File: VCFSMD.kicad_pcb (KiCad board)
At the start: 2 copper layers, 138.4 x 128 mm, 116 parts, among them J1 Conn_01x06_Pin, J10 AudioJack2, J11 AudioJack2, J12 AudioJack2, J13 AudioJack2, J14 Conn_01x06_Pin, J2 Conn_02x05_Odd_Even, J3 Conn_01x07_Pin, J4 Conn_01x07_Pin, J5 AudioJack2, J6 AudioJack2, J7 AudioJack2, J8 AudioJack2, J9 AudioJack2, Q1 BC857, Q2 BC857, Q3 BC847, SW1 SW_SPDT, U1 TL074, U2 L7809, U3 TL074, U4 TL074, U5 LM13700, U6 LM7909_TO220

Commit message: Add files via upload
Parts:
- removed C6, C8: 1u, Capacitor_SMD:C_1206_3216Metric
- removed J1, J14: Conn_01x06_Pin, Connector_PinHeader_2.54mm:PinHeader_1x06_P2.54mm_Vertical
- removed J3, J4: Conn_01x07_Pin, Connector_PinHeader_2.54mm:PinHeader_1x07_P2.54mm_Vertical
- removed U2: L7809, Package_TO_SOT_SMD:SOT-223
- removed U6: LM7909_TO220, Package_TO_SOT_SMD:SOT-223
- added ?: , , F.Cu at (126.6, 63.9)
- added ?: , , F.Cu at (176.2, 63.9)
- added C101: 10u, Capacitor_SMD:C_1206_3216Metric, F.Cu at (181.8, 118.8)
- added C102: 10u, Capacitor_SMD:C_1206_3216Metric, F.Cu at (207.7, 118.5)
- added C103: 10u, Capacitor_SMD:C_1206_3216Metric, F.Cu at (202.6, 118.6)
- added C104: 10u, Capacitor_SMD:C_1206_3216Metric, F.Cu at (184.3, 118.8)
- added J101: Conn_01x08_Pin, Connector_PinSocket_2.54mm:PinSocket_1x08_P2.54mm_Vertical, F.Cu at (182.7, 61.3)
- added J102: Conn_01x09_Pin, Connector_PinHeader_2.54mm:PinHeader_1x09_P2.54mm_Vertical, F.Cu at (127.0, 89.3)
- added J103: Conn_01x09_Pin, Connector_PinHeader_2.54mm:PinHeader_1x09_P2.54mm_Vertical, F.Cu at (176.3, 89.4)
- added J104: Conn_01x08_Pin, Connector_PinSocket_2.54mm:PinSocket_1x08_P2.54mm_Vertical, F.Cu at (133.1, 61.3)
- added R101: 1k, Resistor_SMD:R_1206_3216Metric, F.Cu at (200.1, 118.6)
- added R102: 6k2, Resistor_SMD:R_1206_3216Metric, F.Cu at (205.1, 118.6)
- added R103: 6k2, Resistor_SMD:R_1206_3216Metric, F.Cu at (176.9, 118.8)
- added R104: 1k, Resistor_SMD:R_1206_3216Metric, F.Cu at (179.2, 118.8)
- added U101: LM317_SOT-223, Package_TO_SOT_SMD:SOT-223-3_TabPin2, F.Cu at (204.4, 112.3)
- added U102: LM337_SOT223, Package_TO_SOT_SMD:SOT-223-3_TabPin2, F.Cu at (179.0, 112.4)
- C4, C7, D2, Q3, R12, R28, R31, R35, R4, R42, U3: moved to F.Cu
- moved R28 93.0 mm to (185.2, 48.3), turned to 0 degrees
- moved R12 84.9 mm to (185.2, 46.0), turned to 0 degrees
- moved Q3 83.2 mm to (189.9, 47.0), turned to 180 degrees
- moved C7 79.0 mm to (185.2, 55.1)
- moved R42 78.9 mm to (185.2, 57.6), turned to 180 degrees
- moved R31 78.9 mm to (185.2, 50.7), turned to 0 degrees
- moved D2 78.8 mm to (185.1, 52.9), turned to 180 degrees
- moved C4 73.9 mm to (197.1, 55.7), turned to -90 degrees
- moved R4 71.4 mm to (198.8, 65.0)
- moved R35 67.9 mm to (194.7, 47.1), turned to 0 degrees
- moved U3 57.6 mm to (191.7, 54.2)
- moved D4 5.42 mm to (185.6, 107.5), turned to 180 degrees
- moved R24 5.24 mm to (128.2, 57.7)
- moved RV1 5.11 mm to (131.0, 101.9)
- moved D1 5.11 mm to (139.4, 54.6)
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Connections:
- net Net-(SW1-B) renamed SW12
- C7 pad 1: Net-(C7-Pad1) -> Net-(D2-A)
- C7 pad 2: Net-(D2-A) -> PINGIN
- D11 pad 1: Net-(D11-K) -> GND
- D11 pad 2: Net-(D11-A) -> PINGLED
- J9 pad T: Net-(C7-Pad1) -> PINGIN
- Q3 pad 2: Net-(D11-A) -> Net-(Q3-E)
- R12 pad 1: GND -> PINGLED
- R12 pad 2: Net-(D11-K) -> Net-(Q3-E)
- R42 pad 1: Net-(C7-Pad1) -> PINGIN
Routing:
- net PINGLED: track 0.00 -> 94.2 mm, vias 0 -> 3
- net PINGIN: track 0.00 -> 81.2 mm, vias 0 -> 1
- net BP: track 170.7 -> 118.0 mm, vias 2 -> 5
- net VGNDAUD: track 48.0 -> 11.8 mm, vias 2 -> 0
- net AUDSUM: track 60.9 -> 95.7 mm, vias 0 -> 4
- net GND: track 26.8 -> 58.5 mm, vias 6 -> 8
- net OUT_BP: track 41.2 -> 71.3 mm, vias 1 -> 5
- net OUT_LP: track 34.2 -> 59.8 mm, vias 1 -> 2
- net -9V: track 131.9 -> 155.5 mm, vias 5 -> 7
- net Net-(D11-K): track 22.8 -> 0.00 mm, vias 1 -> 0
- net Net-(U101-ADJ): track 0.00 -> 21.6 mm, vias 0 -> 3
- net Net-(D11-A): track 18.1 -> 0.00 mm, vias 1 -> 0
- net +12V: track 11.5 -> 26.5 mm, vias 0 -> 2
- net AUDIN: track 58.3 -> 72.2 mm
- net +9V: track 31.1 -> 42.5 mm, vias 9 -> 13
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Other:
- board size 138.4 x 128 mm -> 141 x 128 mm

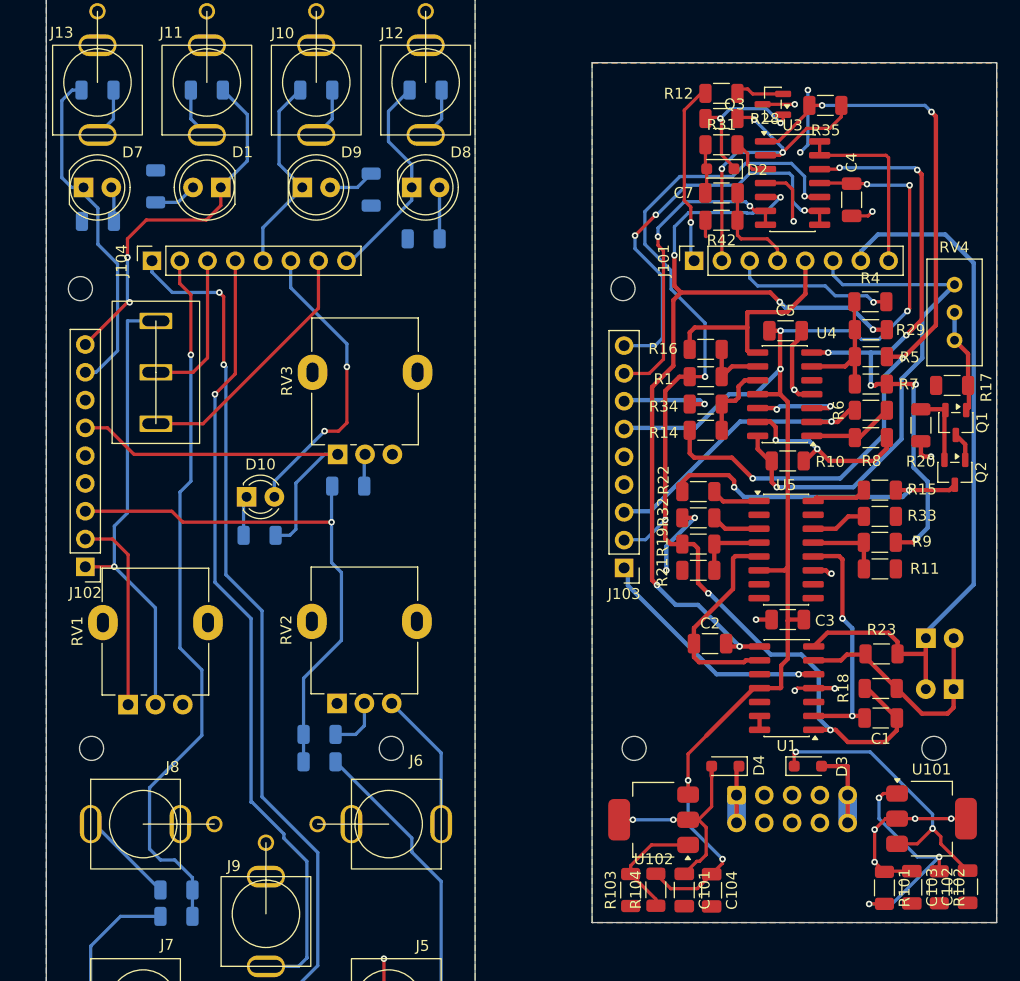
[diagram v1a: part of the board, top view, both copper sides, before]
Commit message: Changed mounting holes for spacers from M2 to M2.5
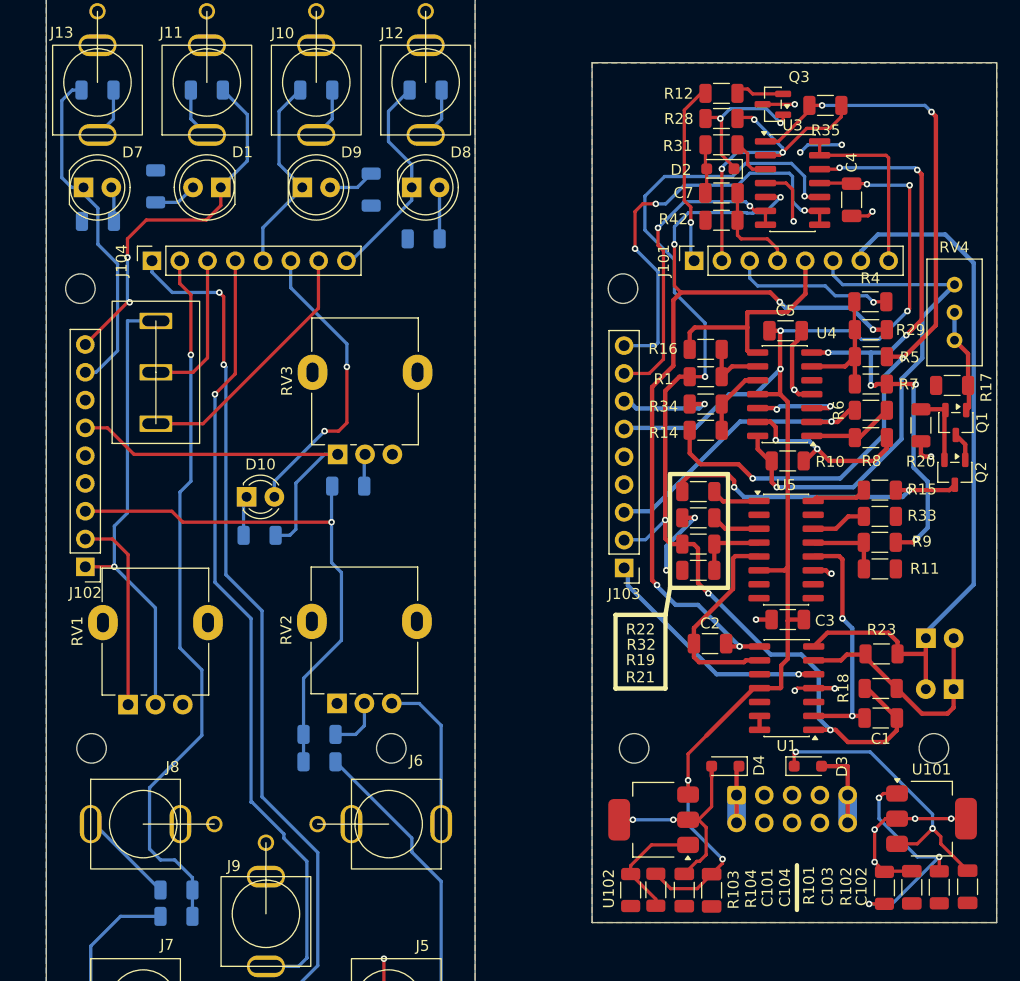
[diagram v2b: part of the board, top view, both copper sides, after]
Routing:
- net GND: track 58.5 -> 55.4 mm
- net Net-(J6-PadT): track 12.9 -> 14.4 mm
- net OUT_BP: track 71.3 -> 72.3 mm
- net BP: track 118.0 -> 118.8 mm

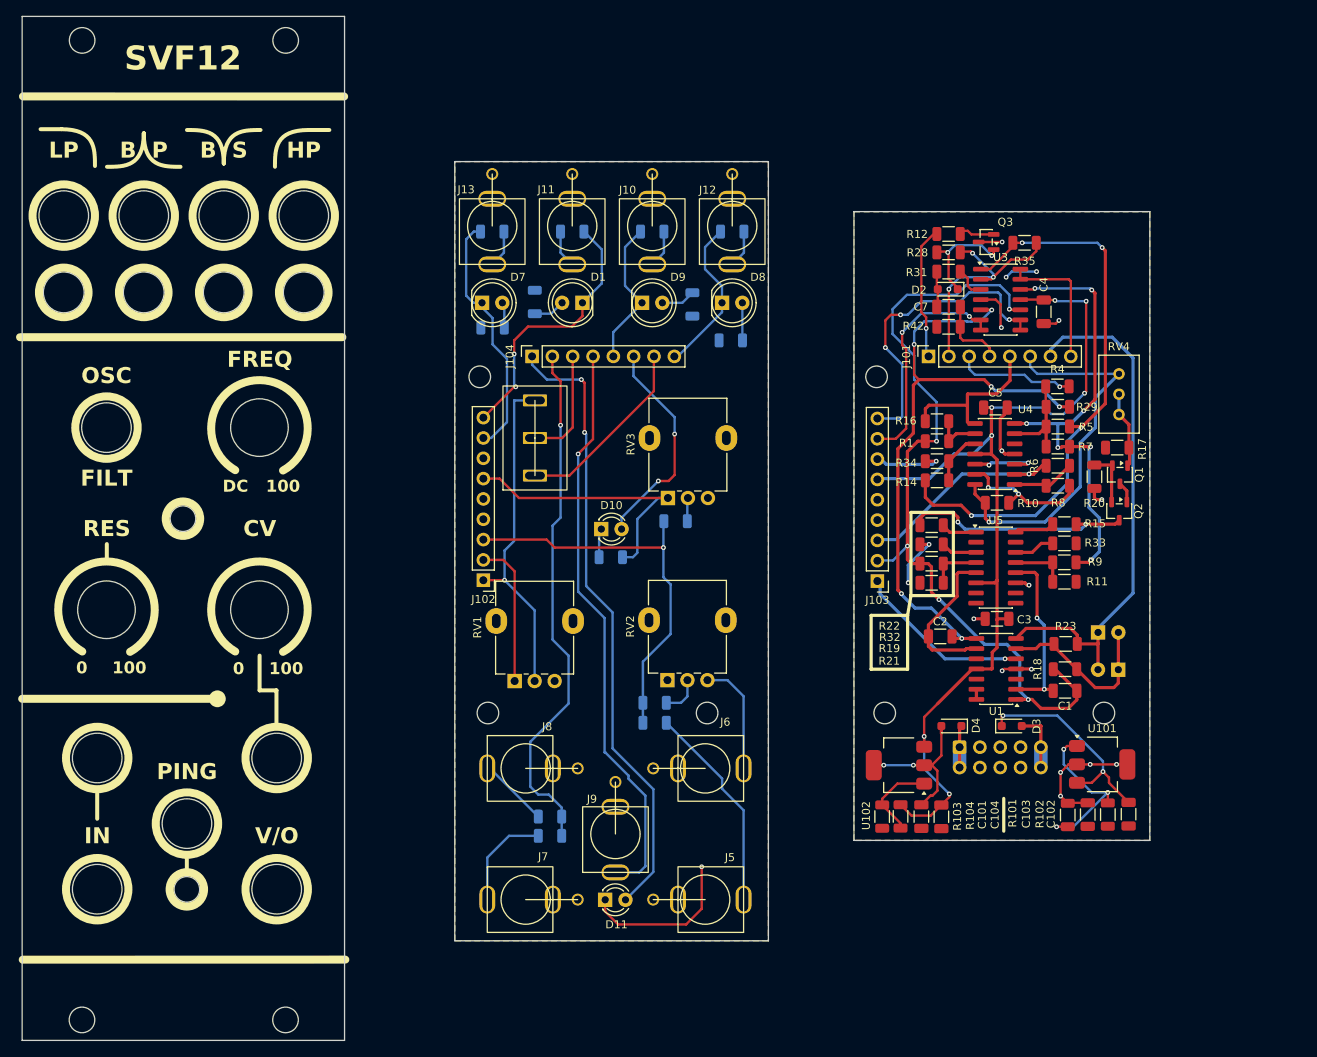
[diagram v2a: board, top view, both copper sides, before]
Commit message: Version 2 with Fixed outputs
The output buffers were driven into phase reversal at high amplitude. Outputs are taken directly out of the filter core.
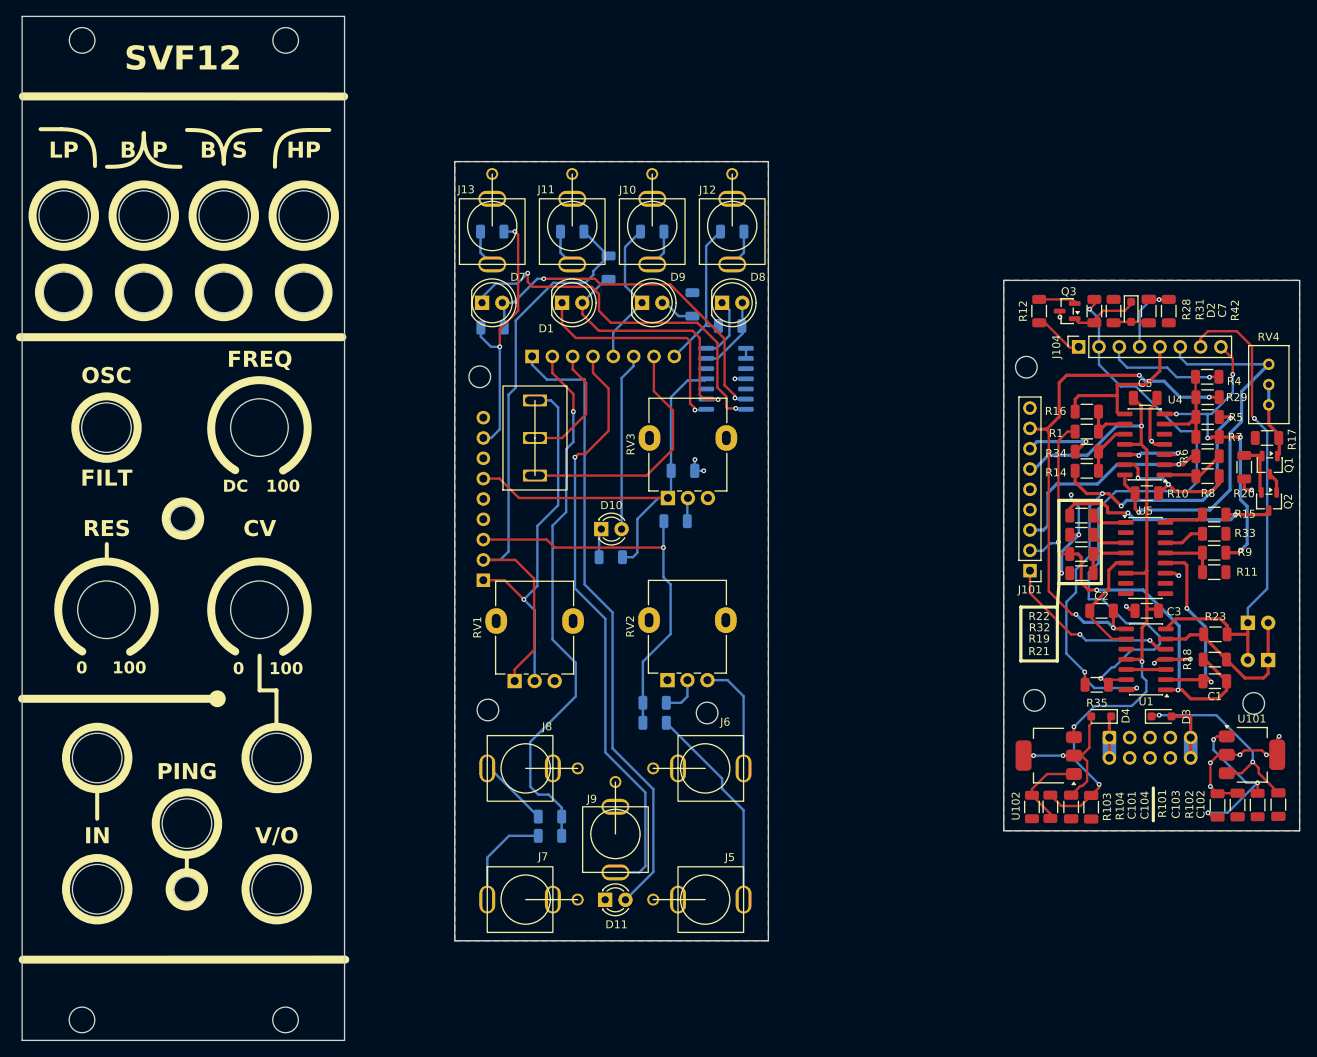
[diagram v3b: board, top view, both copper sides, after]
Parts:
- removed the ? at (177.2, 105.9)
- removed the ? at (176.2, 63.9)
- removed the ? at (204.6, 105.9)
- added ?: , , F.Cu at (195.9, 104.3)
- added ?: , , F.Cu at (194.9, 62.6)
- added ?: , , F.Cu at (223.3, 104.7)
- C4, J103, U3: moved to B.Cu
- J101: value Conn_01x08_Pin -> Conn_01x09_Pin; footprint Connector_PinSocket_2.54mm:PinSocket_1x08_P2.54mm_Vertical -> Connector_PinHeader_2.54mm:PinHeader_1x09_P2.54mm_Vertical
- J102: value Conn_01x09_Pin -> Conn_01x08_Pin; footprint Connector_PinHeader_2.54mm:PinHeader_1x09_P2.54mm_Vertical -> Connector_PinSocket_2.54mm:PinSocket_1x08_P2.54mm_Vertical; moved to B.Cu
- moved J104 68.3 mm to (201.5, 60.1)
- moved R35 56.0 mm to (203.7, 102.3)
- moved C4 49.3 mm to (152.0, 75.6), turned to 0 degrees
- moved J103 49.3 mm to (127.0, 89.3), turned to 0 degrees
- moved U3 35.7 mm to (157.4, 64.1), turned to 180 degrees
- moved J101 29.6 mm to (195.4, 88.1), turned to 180 degrees
- moved J102 28.6 mm to (133.1, 61.3), turned to -90 degrees
- moved R42 27.6 mm to (212.7, 55.6), turned to -90 degrees
- moved C7 25.0 mm to (210.2, 55.6), turned to 90 degrees
- moved D2 23.1 mm to (208.0, 55.7), turned to -90 degrees
- moved R31 21.2 mm to (205.8, 55.6), turned to 90 degrees
- moved C2 20.4 mm to (204.3, 93.1)
- moved R28 19.6 mm to (203.4, 55.6), turned to 90 degrees
- moved C102 18.8 mm to (226.4, 117.3)
- moved C5 18.8 mm to (209.8, 66.5)
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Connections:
- D1 pad 1: OUT_BP -> Net-(D1-KA)
- D7 pad 1: OUT_LP -> Net-(D7-KA)
- D8 pad 1: OUT_HP -> Net-(D8-KA)
- J101 pad 1: PINGLED -> BP_POT
- J101 pad 2: AUDSUM -> BP
- J101 pad 3: SW12 -> VGNDCV
- J101 pad 4: PINGIN -> unconnected-(J101-Pin_4-Pad4)
- J101 pad 5: OUT_BS -> +9V
- J101 pad 6: LED -> -9V
- J101 pad 7: BP_INV -> GND
- J101 pad 8: OUT_HP -> LP
- J102 pad 1: BP_POT -> PINGLED
- J102 pad 2: BP -> AUDSUM
- J102 pad 3: VGNDCV -> SW12
- J102 pad 4: unconnected-(J102-Pin_4-Pad4) -> PINGIN
- J102 pad 5: +9V -> OUT_BS
- J102 pad 6: -9V -> LED
- J102 pad 7: GND -> BP_INV
- J102 pad 8: OUT_LP -> HP
- J103 pad 8: OUT_LP -> LP
- J103 pad 9: OUT_BP -> unconnected-(J103-Pin_9-Pad9)
- J104 pad 8: OUT_HP -> HP
- R24 pad 1: GND -> LP
- R25 pad 1: GND -> HP
- R3 pad 1: GND -> BP
- R39 pad 2: OUT_BP -> BP
- R40 pad 2: OUT_HP -> HP
- R41 pad 2: OUT_LP -> LP
- U1 pad 13: Net-(U1D--) -> AUDSUM
- U1 pad 14: Net-(U1D--) -> AUDIN
- U3 pad 1: AUDIN -> Net-(U3A--)
- U3 pad 10: BP -> GND
- U3 pad 12: HP -> GND
- U3 pad 13: OUT_HP -> Net-(D8-AK)
- U3 pad 14: OUT_HP -> Net-(D8-KA)
- U3 pad 2: AUDSUM -> Net-(U3A--)
- U3 pad 5: LP -> GND
- U3 pad 6: OUT_LP -> Net-(D7-AK)
- U3 pad 7: OUT_LP -> Net-(D7-KA)
- U3 pad 8: OUT_BP -> Net-(D1-KA)
- U3 pad 9: OUT_BP -> Net-(D1-AK)
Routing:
- net OUT_BP: track 72.3 -> 0.00 mm, vias 5 -> 0
- net OUT_LP: track 59.8 -> 0.00 mm, vias 2 -> 0
- net AUDSUM: track 95.7 -> 148.8 mm, vias 4 -> 3
- net Net-(D7-KA): track 0.00 -> 47.2 mm, vias 0 -> 2
- net Net-(D7-AK): track 2.86 -> 44.4 mm, vias 0 -> 2
- net OUT_HP: track 36.6 -> 0.00 mm
- net Net-(D1-KA): track 0.00 -> 29.8 mm, vias 0 -> 1
- net Net-(D1-AK): track 3.98 -> 32.0 mm, vias 0 -> 1
- net LP: track 79.5 -> 98.4 mm
- net GND: track 55.4 -> 37.6 mm, vias 8 -> 6
- net BP: track 118.8 -> 136.4 mm, vias 5 -> 3
- net -9V: track 155.5 -> 143.3 mm, vias 7 -> 4
- net PINGLED: track 94.2 -> 84.3 mm, vias 3 -> 0
- net Net-(D8-KA): track 0.00 -> 8.01 mm
- net Net-(D2-K): track 13.5 -> 8.06 mm, vias 2 -> 0
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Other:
- board size 141 x 128 mm -> 159.7 x 128 mm
